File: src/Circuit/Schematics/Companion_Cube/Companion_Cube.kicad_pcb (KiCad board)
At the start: 2 copper layers, 42.2 x 23.5 mm, 15 parts, among them CON1 AVR-ISP-6, IC1 ATTINY85-S, P1 CONN_11, U1 MINI-B_USB

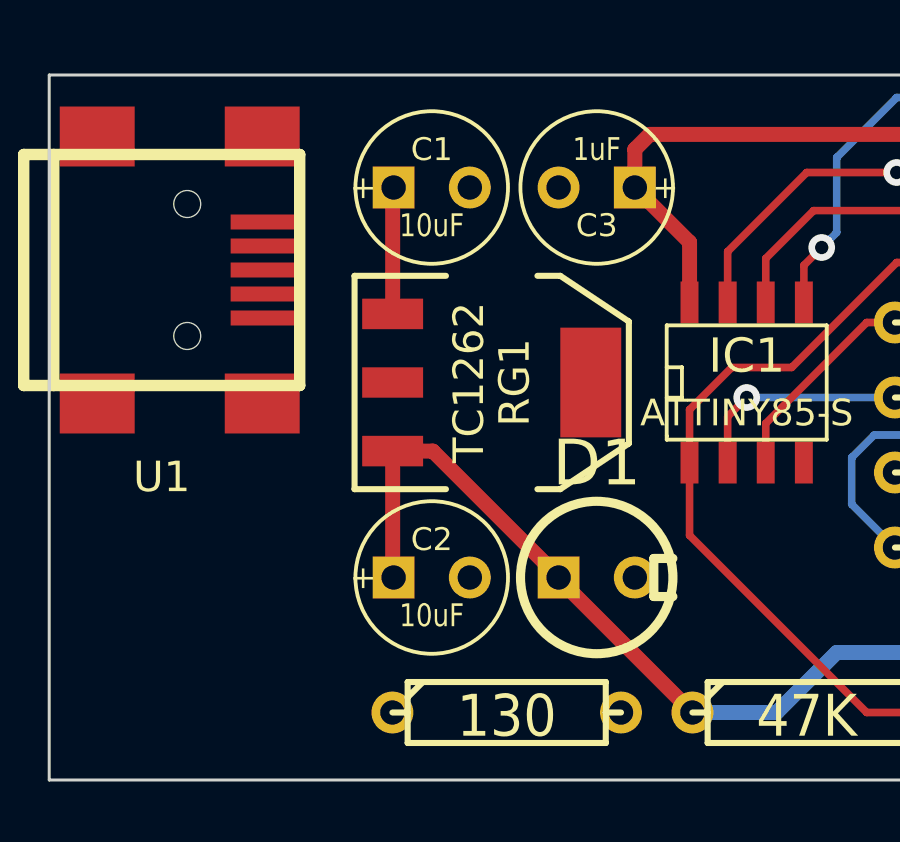
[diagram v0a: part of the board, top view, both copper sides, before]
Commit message: Connected remaining ratsnets, added some logoz
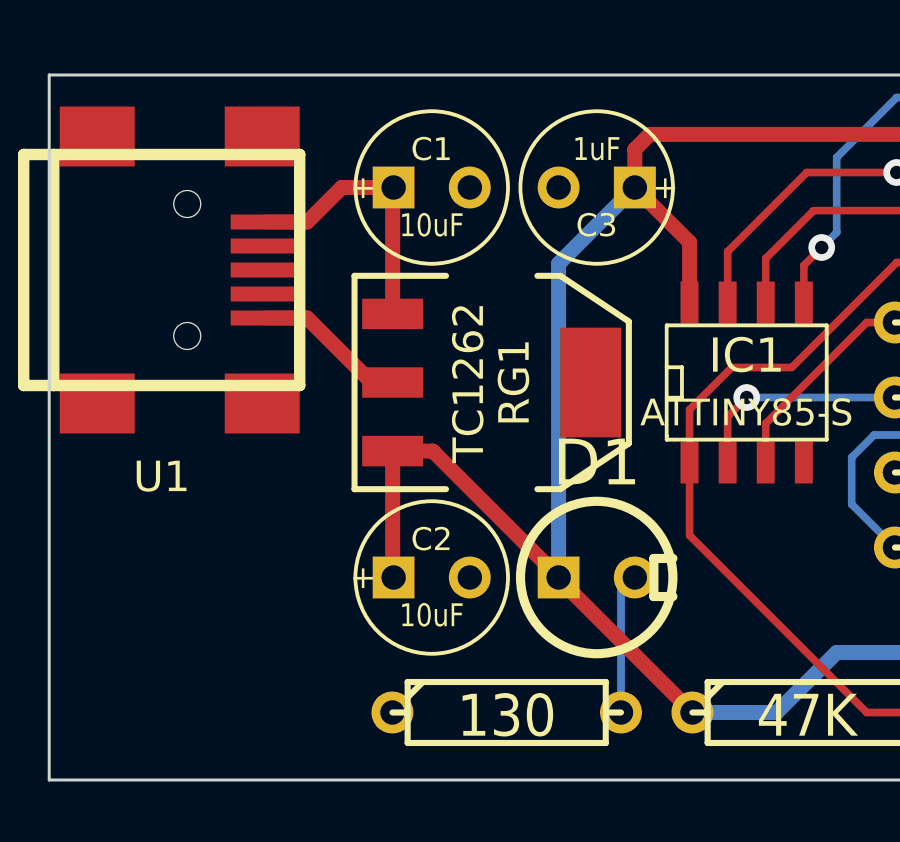
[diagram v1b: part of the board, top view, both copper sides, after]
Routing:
- net VCC: track 53.5 -> 67.6 mm
- net GND: track 0.00 -> 5.14 mm
- net N-0000017: track 4.23 -> 8.98 mm
- net N-0000016: track 0.00 -> 4.69 mm
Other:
- board text added: "Designed By Tyler Hackett 2014"
- board text added: "TASH"
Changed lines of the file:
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@@
   (general
     (links 37)
-    (no_connects 4)
-    (area 197.499956 129.8264 247.20916 154.026401)
+    (no_connects 0)
+    (area 196.321429 129.7871 243.95916 154.800001)
     (thickness 1.6)
-    (drawings 4)
-    (tracks 78)
+    (drawings 6)
+    (tracks 88)
     (zones 0)
     (modules 15)
@@
     )
   )
+  (gr_text "Designed By\nTyler Hackett\n2014" (at 220 141) (layer B.SilkS)
+    (effects (font (size 1.5 1.5) (thickness 0.3)) (justify mirror))
+  )
+  (gr_text TASH (at 202 149 270) (layer F.Mask)
+    (effects (font (size 3 3) (thickness 0.5)))
+  )
   (gr_line (start 242 131.25) (end 199.75 131.25) (angle 90) (layer Edge.Cuts) (width 0.1))
   (gr_line (start 242 154.75) (end 242 131.25) (angle 90) (layer Edge.Cuts) (width 0.1))
   (gr_line (start 199.75 154.75) (end 242 154.75) (angle 90) (layer Edge.Cuts) (width 0.1))
   (gr_line (start 199.75 131.25) (end 199.75 154.75) (angle 90) (layer Edge.Cuts) (width 0.1))
+  (segment (start 206.94932 139.3502) (end 208.3502 139.3502) (width 0.5) (layer F.Cu) (net 1))
+  (segment (start 210.5 141.5) (end 211.198 141.5) (width 0.5) (layer F.Cu) (net 1))
+  (segment (start 208.3502 139.3502) (end 210.5 141.5) (width 0.5) (layer F.Cu) (net 1))
   (segment (start 235.56 147) (end 237.71 147) (width 0.254) (layer B.Cu) (net 2))
   (segment (start 237.71 147) (end 237.98 147.27) (width 0.254) (layer B.Cu) (net 2))
@@
   (segment (start 227 139.5) (end 227.94 139.5) (width 0.254) (layer F.Cu) (net 5))
   (segment (start 223.635 142.865) (end 227 139.5) (width 0.254) (layer F.Cu) (net 5))
+  (segment (start 218.81 152.5) (end 218.81 148.46) (width 0.254) (layer B.Cu) (net 6))
+  (segment (start 218.81 148.46) (end 219.27 148) (width 0.254) (layer B.Cu) (net 6))
+  (segment (start 206.94932 136.1498) (end 208.3502 136.1498) (width 0.5) (layer F.Cu) (net 7))
+  (segment (start 209.5 135) (end 211.23 135) (width 0.5) (layer F.Cu) (net 7))
+  (segment (start 208.3502 136.1498) (end 209.5 135) (width 0.5) (layer F.Cu) (net 7))
   (segment (start 211.198 139.214) (end 211.198 135.032) (width 0.5) (layer F.Cu) (net 7))
   (segment (start 211.198 135.032) (end 211.23 135) (width 0.5) (layer F.Cu) (net 7))
@@
   (segment (start 225 134.5) (end 228 134.5) (width 0.254) (layer F.Cu) (net 13))
   (segment (start 222.365 137.135) (end 225 134.5) (width 0.254) (layer F.Cu) (net 13))
+  (segment (start 216.73 148) (end 216.73 137.54) (width 0.5) (layer B.Cu) (net 14))
+  (segment (start 216.73 137.54) (end 219.27 135) (width 0.5) (layer B.Cu) (net 14))
   (segment (start 237.98 152.35) (end 232.85 152.35) (width 0.5) (layer B.Cu) (net 14))
   (segment (start 224 152.5) (end 221.19 152.5) (width 0.5) (layer B.Cu) (net 14))
@@
   (segment (start 216.73 147.98) (end 212.536 143.786) (width 0.5) (layer F.Cu) (net 14))
   (segment (start 219.27 135) (end 219.27 133.73) (width 0.5) (layer F.Cu) (net 14))
+  (segment (start 219.77 133.23) (end 230.46 133.23) (width 0.5) (layer F.Cu) (net 14))
   (segment (start 219.27 133.73) (end 219.77 133.23) (width 0.5) (layer F.Cu) (net 14))
-  (segment (start 219.77 133.23) (end 230.46 133.23) (width 0.5) (layer F.Cu) (net 14))
   (segment (start 221.095 138.833) (end 221.095 136.825) (width 0.5) (layer F.Cu) (net 14))
   (segment (start 221.095 136.825) (end 219.27 135) (width 0.5) (layer F.Cu) (net 14))

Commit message: Redesigning circuit board for new model
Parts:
- added P2: LED_3, PIN_ARRAY_2X1, F.Cu at (194.3, 120.7)
- added P3: LED_2, PIN_ARRAY_2X1, F.Cu at (209.6, 125.7)
- added P4: LED_1, PIN_ARRAY_2X1, F.Cu at (204.5, 141.0)
- added P5: CONN_1, PIN_ARRAY_1, F.Cu at (209.6, 141.0)
- added P6: CONN_1, PIN_ARRAY_1, F.Cu at (205.7, 144.8)
- added P7: CONN_1, PIN_ARRAY_1, F.Cu at (209.6, 144.8)
- P1: value CONN_11 -> LED_4; footprint pin_array_6x2 -> PIN_ARRAY_2X1
- moved P1 51.0 mm to (189.2, 135.9), turned to 90 degrees
- moved R1 46.7 mm to (189.2, 127.6), turned to 90 degrees
- moved R5 45.2 mm to (196.8, 111.1)
- moved R2 37.7 mm to (202.6, 120.7), turned to 0 degrees
- moved C2 37.2 mm to (194.3, 115.6), turned to 90 degrees
- moved RG1 37.1 mm to (188.0, 115.6), turned to 0 degrees
- moved D1 37.1 mm to (200.0, 115.6), turned to 90 degrees
- moved C1 36.5 mm to (181.6, 115.6), turned to 90 degrees
- moved R4 35.6 mm to (196.2, 141.0)
- moved IC1 27.9 mm to (214.6, 114.9), turned to 90 degrees
- moved R3 23.6 mm to (209.6, 134.0), turned to 270 degrees
- moved U1 23.0 mm to (181.6, 130.8)
- moved CON1 22.1 mm to (216.5, 149.2)
- moved R6 18.1 mm to (207.0, 150.5)
- moved C3 15.1 mm to (213.4, 120.7), turned to 0 degrees
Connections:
- CON1 pad 4: N-000005 (its old number) -> N-000003
- IC1 pad 5: N-000005 (its old number) -> N-000003
- P1 pad 1: N-000004 (its old number) -> GND
- P1 pad 2: GND -> N-0000012
- R1 pad 1: N-000001 -> N-0000012
- R2 pad 1: N-000002 (its old number) -> N-0000011
- R3 pad 1: N-000003 -> N-0000010
- R4 pad 1: N-000004 (its old number) -> N-000008
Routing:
- net VCC: track 67.6 -> 0.00 mm
- net N-000005 (its old number): track 33.8 -> 0.00 mm, vias 1 -> 0
- net N-000002: track 31.5 -> 0.00 mm
- net N-000006: track 25.0 -> 0.00 mm, vias 1 -> 0
- net N-000007: track 23.2 -> 0.00 mm
- net N-0000017: track 8.98 -> 0.00 mm
- net N-000005: track 7.37 -> 0.00 mm, vias 1 -> 0
- net N-000004: track 7.00 -> 0.00 mm
- net GND: track 5.14 -> 0.00 mm
- net N-000009: track 4.69 -> 0.00 mm
- net N-000001: track 2.53 -> 0.00 mm
- net N-000002 (its old number): track 2.52 -> 0.00 mm
- net N-000003: track 2.50 -> 0.00 mm
- net N-000004 (its old number): track 2.48 -> 0.00 mm
- removed copper zone on F.Cu, net GND
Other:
- board size 42.2 x 23.5 mm -> 43.2 x 43.2 mm
- board text removed: "Designed By Tyler Hackett 2014"
- board text removed: "TASH"

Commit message: Connected ratsnet, added some personalization
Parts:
- moved P6 13.7 mm to (218.4, 139.7)
- moved R6 8.91 mm to (215.9, 149.9)
- moved P7 8.13 mm to (215.9, 139.7)
- moved CON1 4.49 mm to (215.9, 144.8)
- moved P5 4.02 mm to (213.4, 139.7)
- moved C3 1.05 mm to (212.3, 120.9), turned to 270 degrees
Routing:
- net N-000007: track 0.00 -> 63.0 mm, vias 0 -> 2
- net VCC: track 0.00 -> 58.7 mm
- net N-000004: track 0.00 -> 48.8 mm, vias 0 -> 1
- net N-000006: track 0.00 -> 41.4 mm, vias 0 -> 1
- net N-000002: track 0.00 -> 34.9 mm
- net N-000003: track 0.00 -> 32.4 mm
- net N-000005: track 0.00 -> 27.7 mm, vias 0 -> 1
- net N-0000017: track 0.00 -> 18.0 mm
- net N-000009: track 0.00 -> 3.44 mm
- net N-0000012: track 0.00 -> 3.18 mm
- net N-0000010: track 0.00 -> 3.18 mm
- net N-000008: track 0.00 -> 3.17 mm
- net N-0000011: track 0.00 -> 3.17 mm
- added copper zone on F.Cu, net GND
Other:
- net class Default: clearance 0.254 -> 0.2032; via_dia 0.889 -> 0.508; via_drill 0.635 -> 0.3302
- net class VCC: trace_width 0.5 -> 0.55
- rule trace_clearance: 0.254 -> 0.2032
- rule via_min_drill: 0.508 -> 0.3302
- rule via_min_size: 0.889 -> 0.508
- board text added: "Designed By Tyler Hackett 2014"
- board text added: "TASH"
